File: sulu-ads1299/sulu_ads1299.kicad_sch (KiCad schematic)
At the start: 20 parts, among them J1 Conn_02x11_Odd_Even, J2 Conn_02x10_Odd_Even, J3 Conn_01x10, J4 Conn_02x07_Odd_Even, J5 73391-0060, J6 Conn_01x02, SW1 SW_Push, U3 S-85S1AB18-I6T1U, U4 S-85S1AB11-I6T1U, U5 LM2775DSG

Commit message: Sulu-ads1299 finalized floorplan, began routing, updated schematic
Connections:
- net 5V_REG renamed +5V_REG
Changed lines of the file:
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@@
     (effects (font (size 1.27 1.27)) (justify left bottom))
-  )
-  (global_label "5V_REG" (shape input) (at 57.15 160.02 0) (fields_autoplaced)
-    (effects (font (size 1.27 1.27)) (justify left))
-    (property "Intersheet References" "${INTERSHEET_REFS}" (id 0) (at 66.5179 159.9406 0)
-      (effects (font (size 1.27 1.27)) (justify left) hide)
-    )
-  )
-  (global_label "5V_REG" (shape input) (at 80.01 81.28 270) (fields_autoplaced)
-    (effects (font (size 1.27 1.27)) (justify right))
-    (property "Intersheet References" "${INTERSHEET_REFS}" (id 0) (at 80.0894 90.6479 90)
-      (effects (font (size 1.27 1.27)) (justify right) hide)
-    )
   )
   (symbol (lib_id "power:GND") (at 172.72 53.34 0) (unit 1)
@@
     (pin "1")
   )
-  (symbol (lib_id "power:PWR_FLAG") (at 251.46 151.13 0) (unit 1)
-    (in_bom yes) (on_board yes)
-    (property "Reference" "#FLG0105" (id 0) (at 251.46 149.225 0)
-      (effects (font (size 1.27 1.27)) hide)
-    )
-    (property "Value" "PWR_FLAG" (id 1) (at 251.46 146.7358 0))
-    (property "Footprint" "" (id 2) (at 251.46 151.13 0)
-      (effects (font (size 1.27 1.27)) hide)
-    )
-    (property "Datasheet" "~" (id 3) (at 251.46 151.13 0)
+  (symbol (lib_id "power:PWR_FLAG") (at 252.73 151.13 0) (unit 1)
+    (in_bom yes) (on_board yes)
+    (property "Reference" "#FLG0105" (id 0) (at 252.73 149.225 0)
+      (effects (font (size 1.27 1.27)) hide)
+    )
+    (property "Value" "PWR_FLAG" (id 1) (at 252.73 146.7358 0))
+    (property "Footprint" "" (id 2) (at 252.73 151.13 0)
+      (effects (font (size 1.27 1.27)) hide)
+    )
+    (property "Datasheet" "~" (id 3) (at 252.73 151.13 0)
       (effects (font (size 1.27 1.27)) hide)
     )
@@
     )
     (property "Datasheet" "" (id 3) (at 123.19 110.49 0)
+      (effects (font (size 1.27 1.27)) hide)
+    )
+    (pin "1")
+  )
+  (symbol (lib_id "draft1library:+5V_REG") (at 265.43 151.13 180) (unit 1)
+    (in_bom yes) (on_board yes)
+    (property "Reference" "#PWR?" (id 0) (at 265.43 147.32 0)
+      (effects (font (size 1.27 1.27)) hide)
+    )
+    (property "Value" "+5V_REG" (id 1) (at 265.0149 155.5099 0))
+    (property "Footprint" "" (id 2) (at 265.43 151.13 0)
+      (effects (font (size 1.27 1.27)) hide)
+    )
+    (property "Datasheet" "" (id 3) (at 265.43 151.13 0)
       (effects (font (size 1.27 1.27)) hide)
     )
@@
     (pin "1")
   )
+  (symbol (lib_id "draft1library:+5V_REG") (at 80.01 81.28 180) (unit 1)
+    (in_bom yes) (on_board yes)
+    (property "Reference" "#PWR?" (id 0) (at 80.01 77.47 0)
+      (effects (font (size 1.27 1.27)) hide)
+    )
+    (property "Value" "+5V_REG" (id 1) (at 85.09 82.55 0))
+    (property "Footprint" "" (id 2) (at 80.01 81.28 0)
+      (effects (font (size 1.27 1.27)) hide)
+    )
+    (property "Datasheet" "" (id 3) (at 80.01 81.28 0)
+      (effects (font (size 1.27 1.27)) hide)
+    )
+    (pin "1")
+  )
   (symbol (lib_id "draft1library:+1.8V_REG") (at 123.19 113.03 270) (unit 1)
     (in_bom yes) (on_board yes)
@@
     (pin "1")
     (pin "2")
+  )
+  (symbol (lib_id "power:PWR_FLAG") (at 265.43 151.13 0) (unit 1)
+    (in_bom yes) (on_board yes)
+    (property "Reference" "#FLG?" (id 0) (at 265.43 149.225 0)
+      (effects (font (size 1.27 1.27)) hide)
+    )
+    (property "Value" "PWR_FLAG" (id 1) (at 265.43 146.7358 0))
+    (property "Footprint" "" (id 2) (at 265.43 151.13 0)
+      (effects (font (size 1.27 1.27)) hide)
+    )
+    (property "Datasheet" "~" (id 3) (at 265.43 151.13 0)
+      (effects (font (size 1.27 1.27)) hide)
+    )
+    (pin "1")
   )
   (symbol (lib_id "draft1library:+VDDIO") (at 123.19 128.27 270) (unit 1)
@@
     (pin "2")
   )
-  (symbol (lib_id "draft1library:+EXT_BAT") (at 251.46 151.13 0) (mirror x) (unit 1)
-    (in_bom yes) (on_board yes)
-    (property "Reference" "#PWR0105" (id 0) (at 251.46 147.32 0)
-      (effects (font (size 1.27 1.27)) hide)
-    )
-    (property "Value" "+EXT_BAT" (id 1) (at 251.841 154.3812 0)
-      (effects (font (size 1.27 1.27)) (justify left))
-    )
-    (property "Footprint" "" (id 2) (at 251.46 151.13 0)
-      (effects (font (size 1.27 1.27)) hide)
-    )
-    (property "Datasheet" "" (id 3) (at 251.46 151.13 0)
+  (symbol (lib_id "draft1library:+EXT_BAT") (at 252.73 151.13 0) (mirror x) (unit 1)
+    (in_bom yes) (on_board yes)
+    (property "Reference" "#PWR0105" (id 0) (at 252.73 147.32 0)
+      (effects (font (size 1.27 1.27)) hide)
+    )
+    (property "Value" "+EXT_BAT" (id 1) (at 248.9192 155.3955 0)
+      (effects (font (size 1.27 1.27)) (justify left))
+    )
+    (property "Footprint" "" (id 2) (at 252.73 151.13 0)
+      (effects (font (size 1.27 1.27)) hide)
+    )
+    (property "Datasheet" "" (id 3) (at 252.73 151.13 0)
       (effects (font (size 1.27 1.27)) hide)
     )
@@
     (pin "1")
   )
+  (symbol (lib_id "draft1library:+5V_REG") (at 57.15 160.02 270) (unit 1)
+    (in_bom yes) (on_board yes)
+    (property "Reference" "#PWR?" (id 0) (at 53.34 160.02 0)
+      (effects (font (size 1.27 1.27)) hide)
+    )
+    (property "Value" "+5V_REG" (id 1) (at 64.77 160.02 90))
+    (property "Footprint" "" (id 2) (at 57.15 160.02 0)
+      (effects (font (size 1.27 1.27)) hide)
+    )
+    (property "Datasheet" "" (id 3) (at 57.15 160.02 0)
+      (effects (font (size 1.27 1.27)) hide)
+    )
+    (pin "1")
+  )
   (symbol (lib_id "draft1library:+VDDIO") (at 110.49 125.73 90) (unit 1)
     (in_bom yes) (on_board yes)
@@
       (reference "#FLG0105") (unit 1) (value "PWR_FLAG") (footprint "")
     )
+    (path "/c8ebdacf-5474-426c-8b44-309a16e51c47"
+      (reference "#FLG?") (unit 1) (value "PWR_FLAG") (footprint "")
+    )
     (path "/b3003d44-e380-408d-b72b-6b879a5b772a"
       (reference "#PWR01") (unit 1) (value "GND") (footprint "")
@@
       (reference "#PWR0115") (unit 1) (value "GND") (footprint "")
     )
+    (path "/aaa1ea39-05b9-470f-96c4-47e6546dd1a7/0d6ef8dd-59bf-4ff2-a038-7ef9ea1da75a"
+      (reference "#PWR?") (unit 1) (value "GND") (footprint "")
+    )
+    (path "/aaa1ea39-05b9-470f-96c4-47e6546dd1a7/1661c7dc-d8ce-4e03-ac67-e270369da1e7"
+      (reference "#PWR?") (unit 1) (value "GND") (footprint "")
+    )
+    (path "/1a2526bb-18a0-4d71-9e39-9be81adefeba"
+      (reference "#PWR?") (unit 1) (value "+5V_REG") (footprint "")
+    )
+    (path "/aaa1ea39-05b9-470f-96c4-47e6546dd1a7/601234f2-df8a-4aa1-8ed1-bd6cd4c3e828"
+      (reference "#PWR?") (unit 1) (value "GND") (footprint "")
+    )
+    (path "/bd6ca432-8e92-48df-8e93-47e28520920a"
+      (reference "#PWR?") (unit 1) (value "+5V_REG") (footprint "")
+    )
+    (path "/fa642c62-5a9e-4a76-8b2d-c1d991d6d25a"
+      (reference "#PWR?") (unit 1) (value "+5V_REG") (footprint "")
+    )
     (path "/710cb968-99ae-463c-8feb-16c0e1c74d6e"
       (reference "C1") (unit 1) (value "2.2 uF") (footprint "Capacitor_SMD:C_0402_1005Metric")
@@
     )
     (path "/aaa1ea39-05b9-470f-96c4-47e6546dd1a7/0fbdf397-369a-438e-be51-0a6f001dc612"
-      (reference "C12") (unit 1) (value "1 uF") (footprint "")
+      (reference "C12") (unit 1) (value "1 uF") (footprint "Capacitor_SMD:C_0402_1005Metric")
     )
     (path "/aaa1ea39-05b9-470f-96c4-47e6546dd1a7/0e92b63d-334c-448f-b0b9-cc1ce2fc8846"
-      (reference "C13") (unit 1) (value "100 uF") (footprint "")
+      (reference "C13") (unit 1) (value "100 uF") (footprint "Capacitor_SMD:C_0402_1005Metric")
     )
     (path "/1f92f92f-1391-4fc3-892c-7c652348c5b5/9c255d8c-5c48-4d75-8385-2b1212a3c0dc"
@@
       (reference "R2") (unit 1) (value "10K") (footprint "Resistor_SMD:R_0402_1005Metric")
     )
-    (path "/aaa1ea39-05b9-470f-96c4-47e6546dd1a7/be1b32b7-2c50-4a43-8148-a90f538b4e56"
-      (reference "R3") (unit 1) (value "10K") (footprint "Resistor_SMD:R_0402_1005Metric")
-    )
     (path "/1f92f92f-1391-4fc3-892c-7c652348c5b5/8a75b756-b700-416a-92f1-b9f47be28c12"

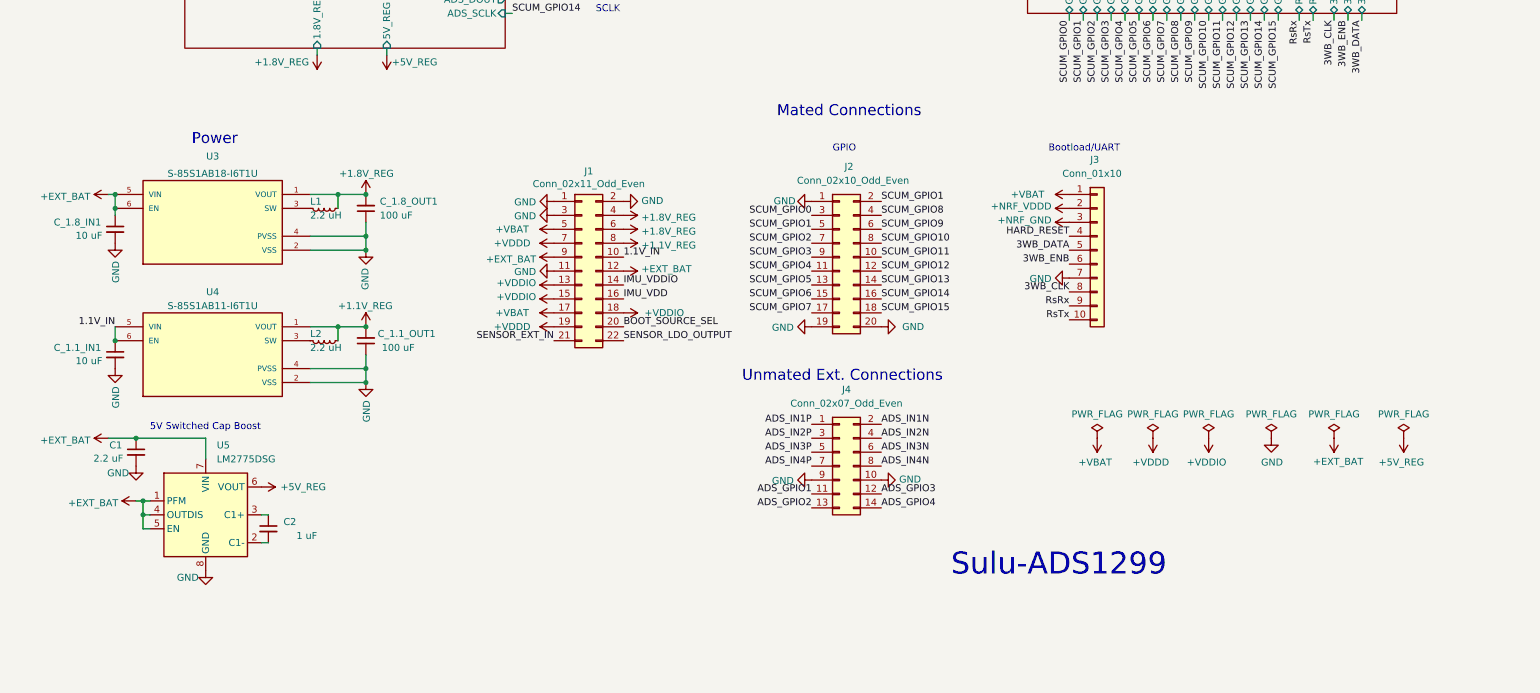
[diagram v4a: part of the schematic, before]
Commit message: Sulu-ads1299 added missing power nets & decap, more routing
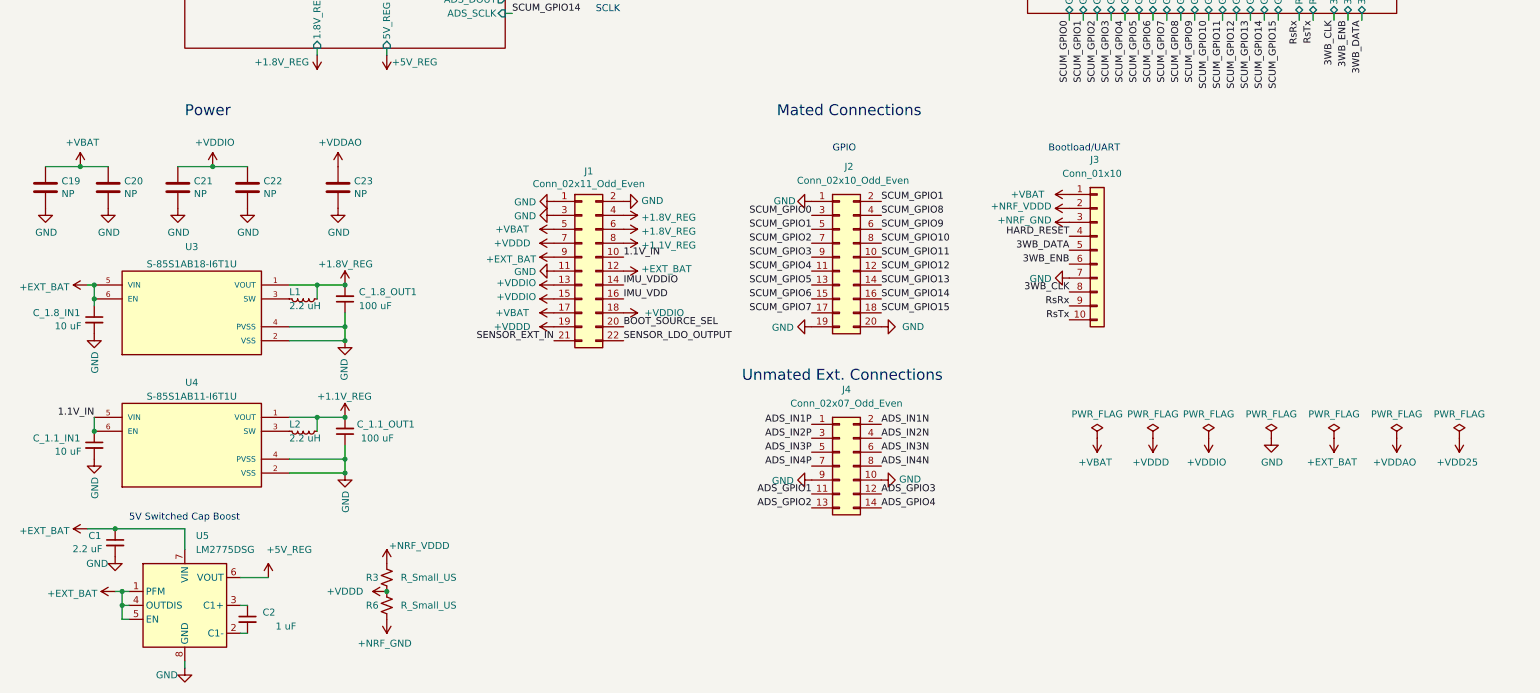
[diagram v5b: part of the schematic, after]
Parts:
- added C19, C20, C21, C22, C23: NP, Capacitor_SMD:C_0402_1005Metric, symbol Device:C
- added R3, R6: R_Small_US, Resistor_SMD:R_0402_1005Metric, symbol Device:R_Small_US
- U3, U4: footprint downloaded_libs:SOFL50P180X50-6N -> SOFL50P180X50-6N
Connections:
- net +NRF_GND: now also R6.2
- net +NRF_VDDD: now also R3.1
- net +VBAT: now also C19.1, C20.1
- net +VDDD: now also R3.2, R6.1
- net +VDDIO: now also C21.1, C22.1
- net GND: now also C19.2, C20.2, C21.2, C22.2, C23.2
- new net +VDDAO: C23.1
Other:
- note removed: "Sulu-ADS1299"
- company: (none) -> Berkeley Sensor and Actuator Center
- title: (none) -> Sulu-ADS1299
- moved on the sheet: C1, C2, C_1.1_IN1, C_1.1_OUT1, C_1.8_IN1, C_1.8_OUT1, L1, L2, U3, U4, U5

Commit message: Sulu-ads1299 layout nearly complete
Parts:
- U3, U4: footprint SOFL50P180X50-6N -> downloaded_libs:SOFL50P180X50-6N
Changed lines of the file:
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@@
+    (effects (font (size 1.27 1.27)) (justify left bottom))
+  )
+  (label "SCUM_GPIO3" (at 102.87 59.69 0)
     (effects (font (size 1.27 1.27)) (justify left bottom))
   )
@@
   (label "SCUM_GPIO0" (at 204.47 74.93 270)
     (effects (font (size 1.27 1.27)) (justify right bottom))
-  )
-  (label "SCUM_GPIO6" (at 102.87 59.69 0)
-    (effects (font (size 1.27 1.27)) (justify left bottom))
   )
   (label "SCUM_GPIO8" (at 224.79 74.93 270)
@@
     (property "Reference" "U3" (id 0) (at 44.45 116.2304 0))
     (property "Value" "S-85S1AB18-I6T1U" (id 1) (at 44.45 119.38 0))
-    (property "Footprint" "SOFL50P180X50-6N" (id 2) (at 44.45 128.27 0)
+    (property "Footprint" "downloaded_libs:SOFL50P180X50-6N" (id 2) (at 44.45 128.27 0)
       (effects (font (size 1.27 1.27)) (justify left bottom) hide)
     )
@@
     (property "Reference" "U4" (id 0) (at 44.45 140.97 0))
     (property "Value" "S-85S1AB11-I6T1U" (id 1) (at 44.45 143.51 0))
-    (property "Footprint" "SOFL50P180X50-6N" (id 2) (at 44.45 152.4 0)
+    (property "Footprint" "downloaded_libs:SOFL50P180X50-6N" (id 2) (at 44.45 152.4 0)
       (effects (font (size 1.27 1.27)) (justify left bottom) hide)
     )
@@
     )
     (path "/05a573af-2182-43b5-975e-54a308809cdf"
-      (reference "U3") (unit 1) (value "S-85S1AB18-I6T1U") (footprint "SOFL50P180X50-6N")
+      (reference "U3") (unit 1) (value "S-85S1AB18-I6T1U") (footprint "downloaded_libs:SOFL50P180X50-6N")
     )
     (path "/f1bb6c0c-a906-4d61-ac80-a54add957e44"
-      (reference "U4") (unit 1) (value "S-85S1AB11-I6T1U") (footprint "SOFL50P180X50-6N")
+      (reference "U4") (unit 1) (value "S-85S1AB11-I6T1U") (footprint "downloaded_libs:SOFL50P180X50-6N")
     )
     (path "/f0b4c895-2bfa-4b95-98c4-800ed43bcfb9"
